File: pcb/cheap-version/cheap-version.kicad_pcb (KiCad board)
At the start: 4 copper layers, 100 x 100 mm, 169 parts, among them J201 UART / 3V3 logic, J301 SHT4x / XH 2.50, J302 FLOAT / 3.5 mm, J401 HRO TF-01A, J501 FAN1 / 3.5 mm, J511 FAN2 / 3.5 mm, J521 PUMP 24V / 6W, J601 PTC + / switched - (3.5 mm), J711 LED +/- (return isolated), J721 LED +/- (return isolated), J731 LED +/- (return isolated), J901 24V IN (KF301-5.0-2P), Q501 AO3400A, Q511 AO3400A, Q521 AO3422, Q601 IRL2505, Q711 BSC146N10LS5, Q721 BSC146N10LS5, SW201 RESET, SW202 BOOT, U101 ST1S10PHR, U201 ESP32-WROOM-32E-N4, U301 PCF8563T/5, U601 IRS4427S, U700 SN74LVC1G08DBVR, U710 AL8853S-13, U720 AL8853S-13, U902 ST1S14PHR, Y301 32.768k 12.5pF

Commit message: Reinforce cheap-version +24V distribution to the LED channels
Replace the 95 mm 0.5 oz In2 +24V loop (2 mm) and the 43 mm 0.5 oz In2
LED2_OUT run with outer-layer copper: +24V crosses the B.Cu +24V_LOADS band
on F.Cu through ten vias, runs as a 3.6 mm B.Cu trunk with branches to the
F711 and F721 feeds (F.Cu pours + via arrays), LED VIN/SW nodes become
pours, LED2_OUT moves to a 1.2 mm B.Cu track.

tools/reinforce_led.py is the repeatable stage, verify_led_copper.py checks
widest continuous filled copper and via counts, freespace.py is the design
aid. DRC with .kicad_dru: 0 errors, 0 unconnected.

Co-Authored-By: Claude Sonnet 5.5 <noreply@anthropic.com>
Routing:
- net +24V: track 199.9 -> 75.7 mm, vias 2 -> 28
- net /LEDDrivers/LED2_OUT: track 102.1 -> 103.9 mm
- added copper zone on F.Cu, net /LEDDrivers/LED1_SW
- added copper zone on F.Cu, net /LEDDrivers/LED1_VIN
- added copper zone on F.Cu, net /LEDDrivers/LED2_SW
- added copper zone on F.Cu, net /LEDDrivers/LED2_VIN

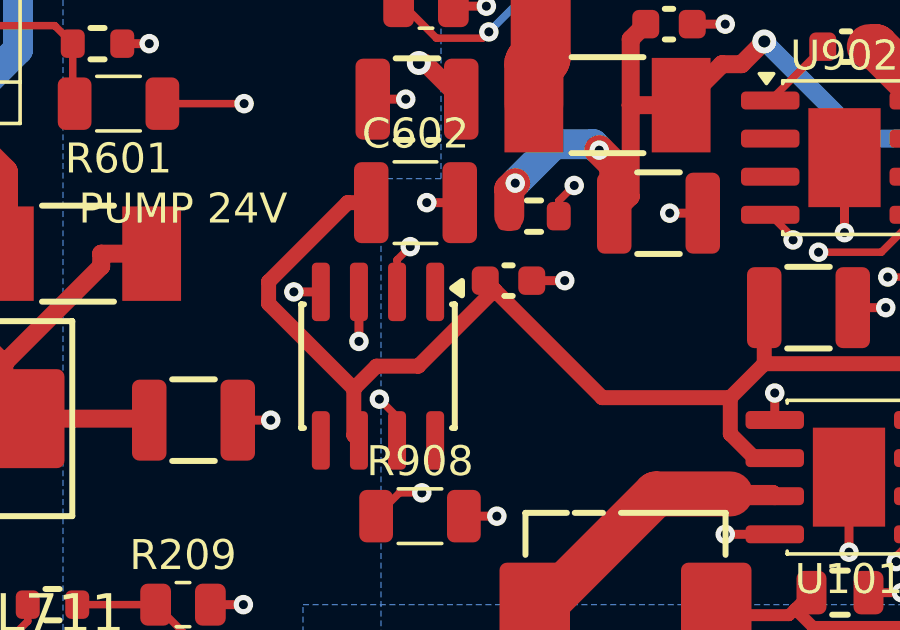
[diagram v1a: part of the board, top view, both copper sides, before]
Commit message: cheap-version: CH1 for 80 W and UCC27524 heater driver
R716 0.18 -> 0.12 ohm (1.667 A, 80 W at 48 V; the LED panel is rated up to
120 W and is not fully loaded). analyze_led_cheap.py re-run: input current
up to 4.61 A, inductor peak 6.26 A, OCP headroom 2.06 A, all model checks
pass; about 96 W is the ceiling of this controller/inductor pair.

U601 is the PCB_V1 UCC27524ADR again instead of the IRS4427S (2.5 V input
threshold left 0.14 V of margin at ESP32 VOH): ENA tied to +12V, ENB to
GND. Board side in tools/swap_heater_driver.py; generator, BOM and BUY
lists follow (order estimate USD 34.69). Schematic ERC 0, schematic and
board match pin by pin.

Co-Authored-By: Claude Sonnet 5.5 <noreply@anthropic.com>
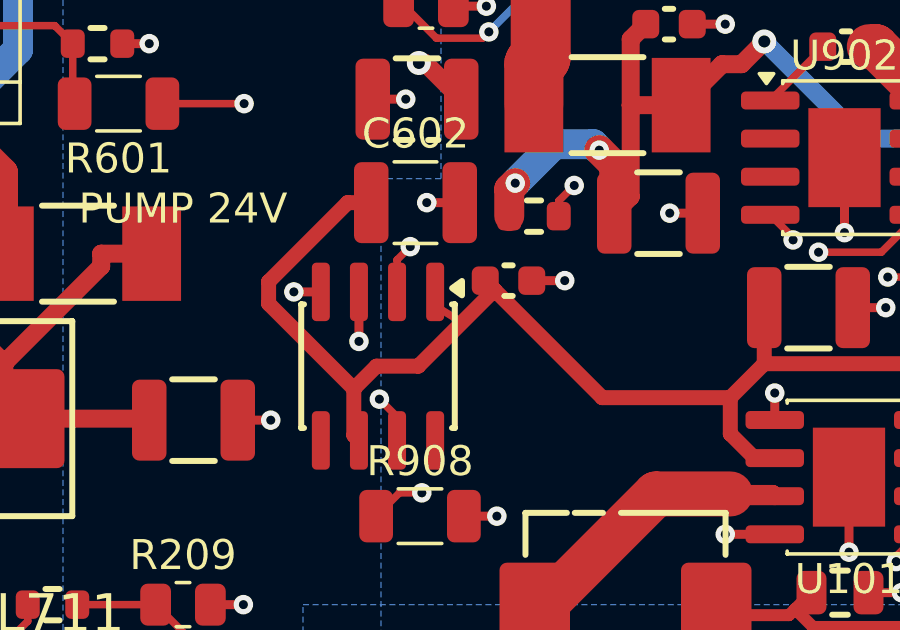
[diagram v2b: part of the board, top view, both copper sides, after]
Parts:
- R716: value 0.18 1% 2W 50ppm -> 0.12 1% 2W 50ppm
- U601: value IRS4427S -> UCC27524ADR
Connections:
- U601 pad 1: unconnected-(U601-NC-Pad1) -> +12V
- U601 pad 8: unconnected-(U601-NC-Pad8) -> GND
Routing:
- net +12V: track 209.9 -> 210.9 mm
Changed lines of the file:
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@@
 			)
 		)
-		(property "Value" "IRS4427S"
+		(property "Value" "UCC27524ADR"
 			(at 0 3.4 270)
 			(layer "F.Fab")
@@
 			)
 		)
-		(property "Datasheet" ""
+		(property "Datasheet" "https://www.ti.com/lit/ds/symlink/ucc27524a.pdf"
 			(at 0 0 270)
 			(layer "F.Fab")
@@
 			)
 		)
-		(property "Manufacturer" "Infineon"
+		(property "Manufacturer" "TI"
 			(at 0 0 270)
 			(layer "F.SilkS")
@@
 			)
 		)
-		(property "MPN" "IRS4427STRPBF"
+		(property "MPN" "UCC27524ADR"
 			(at 0 0 270)
 			(layer "F.SilkS")
@@
 			(layers "F.Cu" "F.Mask" "F.Paste")
 			(roundrect_rratio 0.25)
-			(net "unconnected-(U601-NC-Pad1)")
+			(net "+12V")
 			(pinfunction "ENA_1")
 			(pintype "input")
+			(zone_connect 2)
 		)
 		(pad "2" smd roundrect
@@
 			(layers "F.Cu" "F.Mask" "F.Paste")
 			(roundrect_rratio 0.25)
-			(net "unconnected-(U601-NC-Pad8)")
+			(net "GND")
 			(pinfunction "ENB_8")
 			(pintype "input")
+			(zone_connect 2)
 		)
 		(embedded_fonts no)
@@
 			)
 		)
-		(property "Value" "0.18 1% 2W 50ppm"
+		(property "Value" "0.12 1% 2W 50ppm"
 			(at 0 2.63 90)
 			(layer "F.Fab")
@@
 			)
 		)
-		(property "MPN" "FRM252WFR180TM"
+		(property "MPN" "FRM252WFR120TM"
 			(at 0 0 90)
 			(layer "F.SilkS")
@@
 			)
 		)
-		(property "LCSC" "C48533605"
+		(property "LCSC" ""
 			(at 0 0 90)
 			(layer "F.SilkS")
@@
 		(layer "F.Cu")
 		(net "+12V")
+	)
+	(segment
+		(start 83.5 90.3)
+		(end 84.3 90.79)
+		(width 0.25)
+		(locked yes)
+		(layer "F.Cu")
+		(net "+12V")
